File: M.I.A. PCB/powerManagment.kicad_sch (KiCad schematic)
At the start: 43 parts, among them J14 Screw_Terminal_01x02, J18 Screw_Terminal_01x02, J2 Conn_01x02_Pin, U10 AP2112K-3.3, U11 INA219AxDCN, U12 AP62150WU, U13 TPS2121RUXR, U14 AP62150WU, U9 TPS2121RUXR

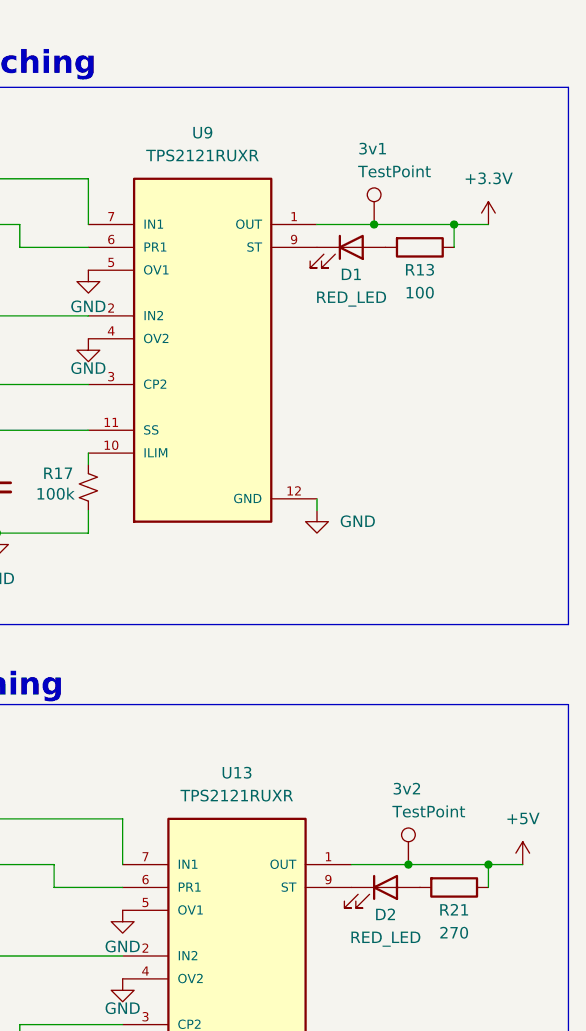
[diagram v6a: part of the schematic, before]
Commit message: Routed two ignition lines
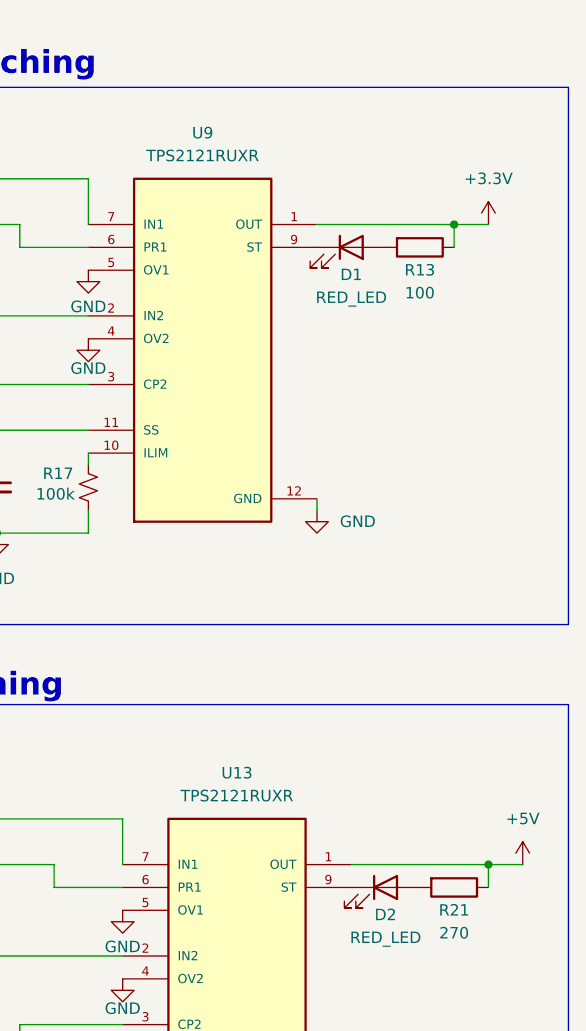
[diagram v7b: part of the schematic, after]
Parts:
- removed 3v1, 3v2: TestPoint, TestPoint:TestPoint_Pad_D1.0mm, symbol Connector:TestPoint
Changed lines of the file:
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@@
 	)
 	(junction
-		(at 262.89 114.3)
-		(diameter 0)
-		(color 0 0 0 0)
-	)
-	(junction
 		(at 149.86 82.55)
 		(diameter 0)
@@
 	)
 	(junction
-		(at 259.08 43.18)
-		(diameter 0)
-		(color 0 0 0 0)
-	)
-	(junction
 		(at 35.56 104.14)
 		(diameter 0)
@@
 	(wire
 		(pts
-			(xy 259.08 43.18) (xy 267.97 43.18)
-		)
-		(stroke
-			(width 0)
-			(type default)
-		)
-	)
-	(wire
-		(pts
 			(xy 59.69 68.58) (xy 59.69 74.93)
 		)
@@
 	(wire
 		(pts
-			(xy 262.89 114.3) (xy 271.78 114.3)
+			(xy 256.54 114.3) (xy 271.78 114.3)
 		)
 		(stroke
@@
 	(wire
 		(pts
-			(xy 252.73 43.18) (xy 259.08 43.18)
+			(xy 252.73 43.18) (xy 267.97 43.18)
 		)
 		(stroke
@@
 	(wire
 		(pts
-			(xy 256.54 114.3) (xy 262.89 114.3)
-		)
-		(stroke
-			(width 0)
-			(type default)
-		)
-	)
-	(wire
-		(pts
 			(xy 227.33 38.1) (xy 227.33 43.18)
 		)
@@
 	)
 	(symbol
-		(lib_id "Connector:TestPoint")
-		(at 262.89 114.3 0)
-		(unit 1)
-		(exclude_from_sim no)
-		(in_bom yes)
-		(on_board yes)
-		(dnp no)
-		(property "Reference" "3v2"
-			(at 261.112 105.918 0)
-			(effects
-				(font
-					(size 1.27 1.27)
-				)
-				(justify left)
-			)
-		)
-		(property "Value" "TestPoint"
-			(at 261.112 108.458 0)
-			(effects
-				(font
-					(size 1.27 1.27)
-				)
-				(justify left)
-			)
-		)
-		(property "Footprint" "TestPoint:TestPoint_Pad_D1.0mm"
-			(at 267.97 114.3 0)
-			(effects
-				(font
-					(size 1.27 1.27)
-				)
-				(hide yes)
-			)
-		)
-		(property "Datasheet" "~"
-			(at 267.97 114.3 0)
-			(effects
-				(font
-					(size 1.27 1.27)
-				)
-				(hide yes)
-			)
-		)
-		(property "Description" "test point"
-			(at 262.89 114.3 0)
-			(effects
-				(font
-					(size 1.27 1.27)
-				)
-				(hide yes)
-			)
-		)
-		(property "LCSC" ""
-			(at 262.89 114.3 0)
-			(effects
-				(font
-					(size 1.27 1.27)
-				)
-				(hide yes)
-			)
-		)
-		(property "Manufacturer" ""
-			(at 262.89 114.3 0)
-			(effects
-				(font
-					(size 1.27 1.27)
-				)
-				(hide yes)
-			)
-		)
-		(property "Manufacturer Part" ""
-			(at 262.89 114.3 0)
-			(effects
-				(font
-					(size 1.27 1.27)
-				)
-				(hide yes)
-			)
-		)
-		(pin "1"
-		)
-		(instances
-			(project "M.I.A."
-				(path "/4d55825e-4251-44bf-9376-9abd9228f348/54343a2d-63f4-495d-8740-a310821afec1"
-					(reference "3v2")
-					(unit 1)
-				)
-			)
-		)
-	)
-	(symbol
 		(lib_id "power:GND")
 		(at 227.33 48.26 0)
@@
 					(unit 1)
 				)
-			)
-		)
-	)
-	(symbol
-		(lib_id "Connector:TestPoint")
-		(at 259.08 43.18 0)
-		(unit 1)
-		(exclude_from_sim no)
-		(in_bom yes)
-		(on_board yes)
-		(dnp no)
-		(property "Reference" "3v1"
-			(at 257.302 34.798 0)
-			(effects
-				(font
-					(size 1.27 1.27)
-				)
-				(justify left)
-			)
-		)
-		(property "Value" "TestPoint"
-			(at 257.302 37.338 0)
-			(effects
-				(font
-					(size 1.27 1.27)
-				)
-				(justify left)
-			)
-		)
-		(property "Footprint" "TestPoint:TestPoint_Pad_D1.0mm"
-			(at 264.16 43.18 0)
-			(effects
-				(font
-					(size 1.27 1.27)
-				)
-				(hide yes)
-			)
-		)
-		(property "Datasheet" "~"
-			(at 264.16 43.18 0)
-			(effects
-				(font
-					(size 1.27 1.27)
-				)
-				(hide yes)
-			)
-		)
-		(property "Description" "test point"
-			(at 259.08 43.18 0)
-			(effects
-				(font
-					(size 1.27 1.27)
-				)
-				(hide yes)
-			)
-		)
-		(property "LCSC" ""
-			(at 259.08 43.18 0)
-			(effects
-				(font
-					(size 1.27 1.27)
-				)
-				(hide yes)
-			)
-		)
-		(property "Manufacturer" ""
-			(at 259.08 43.18 0)
-			(effects
-				(font
-					(size 1.27 1.27)
-				)
-				(hide yes)
-			)
-		)
-		(property "Manufacturer Part" ""
-			(at 259.08 43.18 0)
-			(effects
-				(font
-					(size 1.27 1.27)
-				)
-				(hide yes)
-			)
-		)
-		(pin "1"
-		)
-		(instances
-			(project "M.I.A."
-				(path "/4d55825e-4251-44bf-9376-9abd9228f348/54343a2d-63f4-495d-8740-a310821afec1"
-					(reference "3v1")
-					(unit 1)
-				)

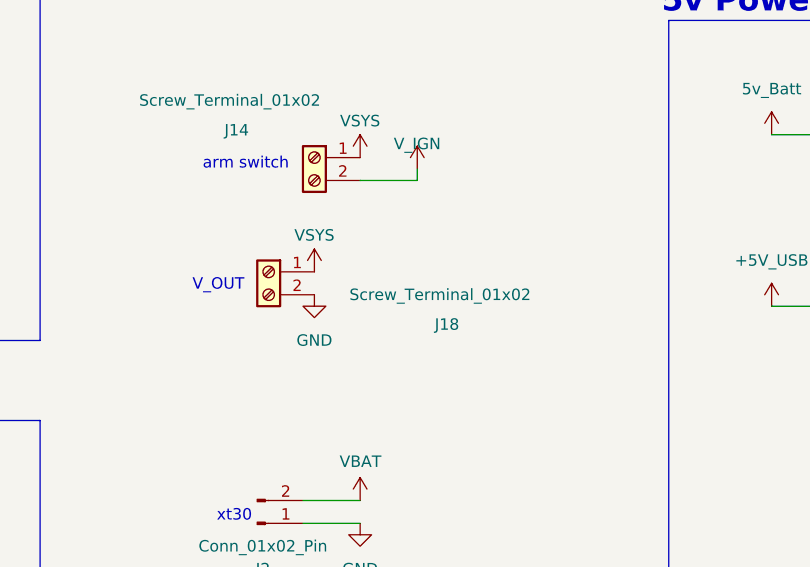
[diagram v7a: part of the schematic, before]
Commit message: Added LEDs, Prepped for 4 layer conversion
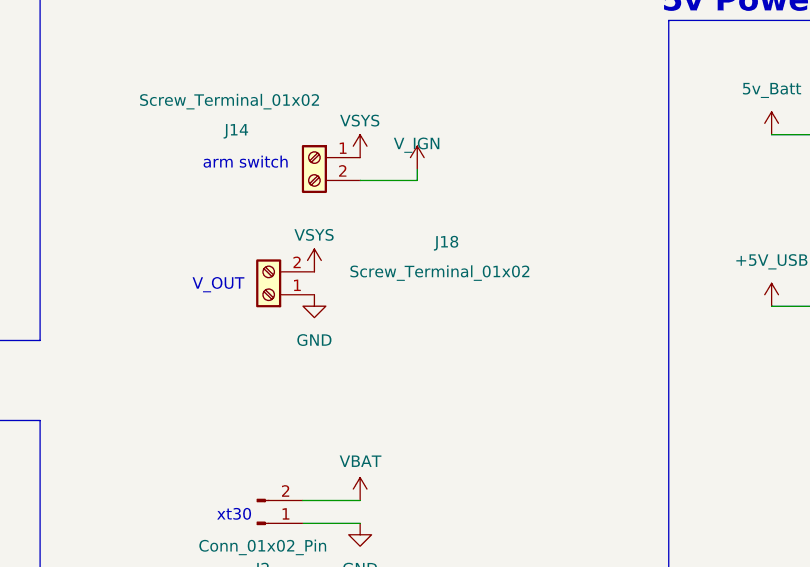
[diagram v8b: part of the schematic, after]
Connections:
- net GND: now also J18.1 (Pin_1); no longer J18.2 (Pin_2)
- net VSYS: now also J18.2 (Pin_2); no longer J18.1 (Pin_1)
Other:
- moved on the sheet: J18
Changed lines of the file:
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@@
 	(symbol
 		(lib_id "Connector:Screw_Terminal_01x02")
-		(at 142.24 124.46 0)
-		(mirror y)
+		(at 142.24 127 180)
 		(unit 1)
 		(exclude_from_sim no)
@@
 		(dnp no)
 		(property "Reference" "J18"
-			(at 162.052 130.302 0)
+			(at 162.052 121.158 0)
 			(effects
 				(font
@@
 		)
 		(property "Value" "Screw_Terminal_01x02"
-			(at 161.29 127 0)
+			(at 161.29 124.46 0)
 			(effects
 				(font
@@
 		)
 		(property "Footprint" "PCM_SparkFun-Connector:ScrewTerminal_1x02_P3.5mm_Horizontal_Black"
-			(at 142.24 124.46 0)
+			(at 142.24 127 0)
 			(effects
 				(font
@@
 		)
 		(property "Datasheet" "~"
-			(at 142.24 124.46 0)
+			(at 142.24 127 0)
 			(effects
 				(font
@@
 		)
 		(property "Description" "Generic screw terminal, single row, 01x02, script generated (kicad-library-utils/schlib/autogen/connector/)"
-			(at 142.24 124.46 0)
+			(at 142.24 127 0)
 			(effects
 				(font
